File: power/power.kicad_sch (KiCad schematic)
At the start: 9 parts, among them J1 GPIO, J2 PWM, J3 Conn_01x16, J4 JP_EXT, Q1 D15P05

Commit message: move buzzer to power board
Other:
- added sheet Buzzer (_buzzer.kicad_sch)
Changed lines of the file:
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@@
 	(text "PWM Connector"
 		(exclude_from_sim no)
-		(at 356.0465 24.384 0)
+		(at 356.235 24.13 0)
 		(effects
 			(font
@@
 	(text "Connected to battery"
 		(exclude_from_sim no)
-		(at 145.288 128.524 0)
+		(at 145.415 128.27 0)
 		(effects
 			(font
@@
 	(text "Additional pin functions:\nhttps://pinout.xyz/"
 		(exclude_from_sim no)
-		(at 301.498 258.572 0)
+		(at 301.625 258.445 0)
 		(effects
 			(font
@@
 	(text "Power LED"
 		(exclude_from_sim no)
-		(at 293.624 112.014 0)
+		(at 293.37 111.76 0)
 		(effects
 			(font
@@
 	(text "Connector for unused RPi pins"
 		(exclude_from_sim no)
-		(at 189.992 24.13 0)
+		(at 189.865 24.13 0)
 		(effects
 			(font
@@
 	(text "RPi HAT connector"
 		(exclude_from_sim no)
-		(at 42.418 23.114 0)
+		(at 42.545 22.86 0)
 		(effects
 			(font
@@
 	(wire
 		(pts
+			(xy 64.77 138.43) (xy 68.58 138.43)
+		)
+		(stroke
+			(width 0)
+			(type default)
+		)
+	)
+	(wire
+		(pts
 			(xy 222.25 119.38) (xy 222.25 114.3)
 		)
@@
 		)
 	)
+	(label "GPIO12{slash}PWM0"
+		(at 68.58 138.43 0)
+		(effects
+			(font
+				(size 1.27 1.27)
+			)
+			(justify left bottom)
+		)
+	)
 	(label "PWM1"
 		(at 354.33 64.77 0)
@@
 				)
 			)
+		)
+	)
+	(sheet
+		(at 30.48 124.46)
+		(size 34.29 26.67)
+		(exclude_from_sim no)
+		(in_bom yes)
+		(on_board yes)
+		(dnp no)
+		(fields_autoplaced yes)
+		(stroke
+			(width 0.1524)
+			(type solid)
+		)
+		(fill
+			(color 0 0 0 0)
+		)
+		(property "Sheetname" "Buzzer"
+			(at 30.48 123.7484 0)
+			(show_name no)
+			(do_not_autoplace no)
+			(effects
+				(font
+					(size 1.27 1.27)
+				)
+				(justify left bottom)
+			)
+		)
+		(property "Sheetfile" "_buzzer.kicad_sch"
+			(at 30.48 151.0796 0)
+			(show_name no)
+			(do_not_autoplace no)
+			(effects
+				(font
+					(size 1.27 1.27)
+				)
+				(justify left top)
+			)
+		)
+		(pin "PWM" input
+			(at 64.77 138.43 0)
+			(effects
+				(font
+					(size 1.27 1.27)
+				)
+				(justify right)
+			)
+		)
+		(instances
+			(project "power"
+				(path "/e63e39d7-6ac0-4ffd-8aa3-1841a4541b55"
+					(page "3")
+				)
+			)

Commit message: add buzzer bridged with jumper
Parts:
- added JP1: JP_BUZZ_PWM, Connector_PinHeader_2.54mm:PinHeader_1x02_P2.54mm_Vertical, symbol Jumper:Jumper_2_Open
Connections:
- net GPIO12/PWM0: now also JP1.2 (B)
- new net Buzzer/PWM: JP1.1 (A)
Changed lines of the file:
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@@
+	(wire
+		(pts
+			(xy 78.74 138.43) (xy 85.09 138.43)
+		)
+		(stroke
+			(width 0)
+			(type default)
+		)
+	)
 	(wire
 		(pts
@@
 	)
 	(label "GPIO12{slash}PWM0"
-		(at 68.58 138.43 0)
+		(at 85.09 138.43 0)
 		(effects
 			(font
@@
 					(unit 1)
 				)
+			)
+		)
+	)
+	(symbol
+		(lib_id "Jumper:Jumper_2_Open")
+		(at 73.66 138.43 0)
+		(unit 1)
+		(body_style 1)
+		(exclude_from_sim no)
+		(in_bom yes)
+		(on_board yes)
+		(in_pos_files yes)
+		(dnp no)
+		(fields_autoplaced yes)
+		(property "Reference" "JP1"
+			(at 73.66 132.08 0)
+			(show_name no)
+			(do_not_autoplace no)
+			(effects
+				(font
+					(size 1.27 1.27)
+				)
+			)
+		)
+		(property "Value" "JP_BUZZ_PWM"
+			(at 73.66 134.62 0)
+			(show_name no)
+			(do_not_autoplace no)
+			(effects
+				(font
+					(size 1.27 1.27)
+				)
+			)
+		)
+		(property "Footprint" "Connector_PinHeader_2.54mm:PinHeader_1x02_P2.54mm_Vertical"
+			(at 73.66 138.43 0)
+			(hide yes)
+			(show_name no)
+			(do_not_autoplace no)
+			(effects
+				(font
+					(size 1.27 1.27)
+				)
+			)
+		)
+		(property "Datasheet" ""
+			(at 73.66 138.43 0)
+			(hide yes)
+			(show_name no)
+			(do_not_autoplace no)
+			(effects
+				(font
+					(size 1.27 1.27)
+				)
+			)
+		)
+		(property "Description" "Jumper, 2-pole, open"
+			(at 73.66 138.43 0)
+			(hide yes)
+			(show_name no)
+			(do_not_autoplace no)
+			(effects
+				(font
+					(size 1.27 1.27)
+				)
+			)
+		)
+		(property "Part" ""
+			(at 73.66 138.43 0)
+			(hide yes)
+			(show_name no)
+			(do_not_autoplace no)
+			(effects
+				(font
+					(size 1.27 1.27)
+				)
+			)
+		)
+		(pin "1"
+		)
+		(pin "2"
+		)
+		(instances
+			(project "power"
+				(path "/e63e39d7-6ac0-4ffd-8aa3-1841a4541b55"
+					(reference "JP1")
+					(unit 1)
+				)

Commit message: lots of changes
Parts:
- added J5: JP_VOLTS, Connector_PinSocket_2.54mm:PinSocket_1x02_P2.54mm_Vertical, symbol Connector:Conn_01x02_Socket
- D2: value LED -> LED_RED
- J1: Part (none) -> 2541FV-2x20P-B
- J2: value PWM -> PWM_OUT
- J3: value Conn_01x16 -> PWM_IN; footprint Connector_PinHeader_2.54mm:PinHeader_1x16_P2.54mm_Vertical -> Connector_PinSocket_2.54mm:PinSocket_1x16_P2.54mm_Vertical; Part (none) -> 2541FV-16P-B
- J4: footprint Connector_PinHeader_2.54mm:PinHeader_2x08_P2.54mm_Horizontal -> Connector_PinHeader_2.54mm:PinHeader_2x08_P2.54mm_Vertical; Part (none) -> 2011-2X08G00RB
- JP1: Part (none) -> 2541WV-2X01P
- Q1: Part (none) -> RFD15P05SM-VB
- R3: Part (none) -> RCA0520KFLF
- R4: Part (none) -> RCA0510KFLF
- R5: Part (none) -> SCR0805F1K
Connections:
- new net BATT_VDIV: J5.2 (Pin_2)
- new net VREF: J5.1 (Pin_1)
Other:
- added sheet V-Div (_vdiv.kicad_sch)
- added sheet V-Ref (_vref.kicad_sch)
- note added: "Voltages to sensor board"
- moved on the sheet: D2, JP1, Q1, R3, R4, R5

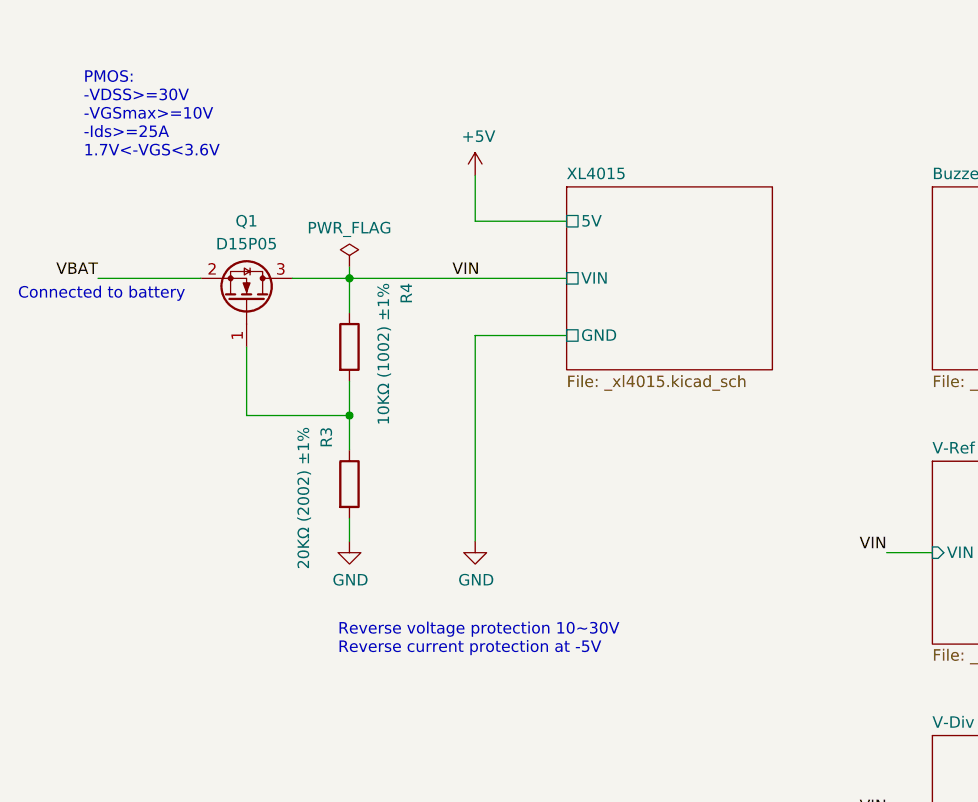
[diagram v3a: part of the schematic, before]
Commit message: initial TPS56A37 DCDC attempt
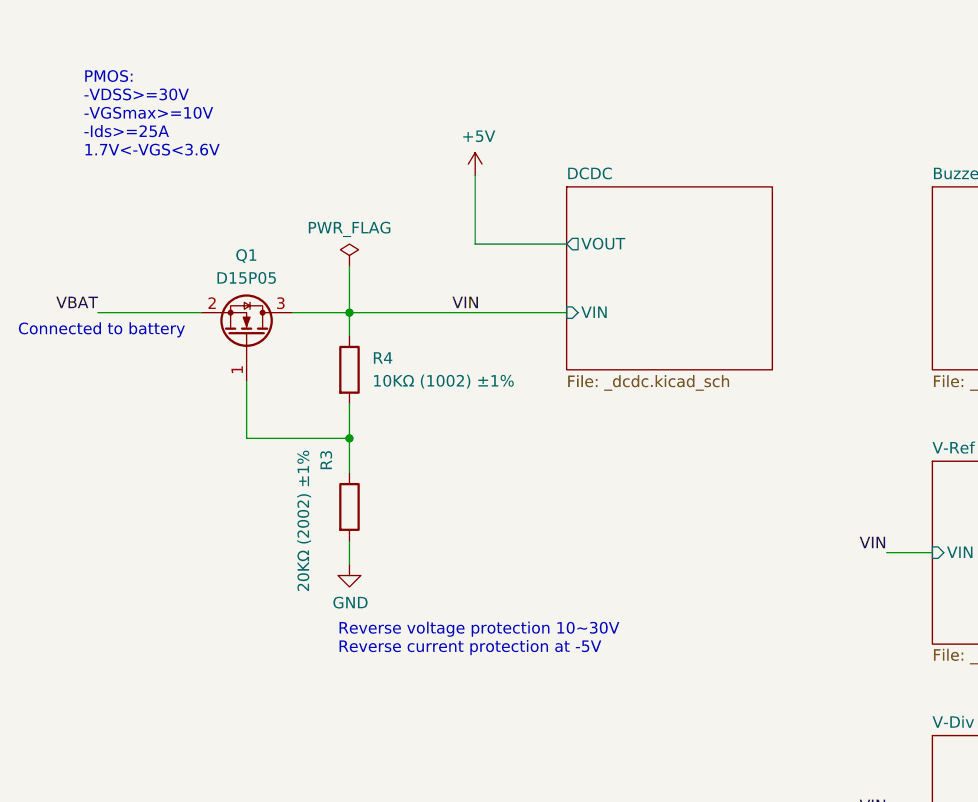
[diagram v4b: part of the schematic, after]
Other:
- removed sheet XL4015
- added sheet DCDC (_dcdc.kicad_sch)
- moved on the sheet: Q1, R3, R4
